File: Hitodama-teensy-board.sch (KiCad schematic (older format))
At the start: 16 parts, among them J1 Jack-DC, J2 Conn_01x20_Female, J3 Conn_01x20_Female, J4 Conn_01x20_Female, U4 Teensy3.6

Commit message: 2 row connector, routed on intermediate board
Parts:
- J2, J3, J4: footprint Connector_PinHeader_2.54mm:PinHeader_1x20_P2.54mm_Vertical -> Connector_IDC:IDC-Header_2x10_P2.54mm_Vertical
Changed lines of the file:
@@
 F 0 "J2" V 2265 4480 50  0000 C CNN
 F 1 "Conn_01x20_Female" V 2174 4480 50  0000 C CNN
-F 2 "Connector_PinHeader_2.54mm:PinHeader_1x20_P2.54mm_Vertical" H 2100 4550 50  0001 C CNN
+F 2 "Connector_IDC:IDC-Header_2x10_P2.54mm_Vertical" H 2100 4550 50  0001 C CNN
 F 3 "~" H 2100 4550 50  0001 C CNN
 	1    2100 4550
@@
 F 0 "J3" V 2265 5530 50  0000 C CNN
 F 1 "Conn_01x20_Female" V 2174 5530 50  0000 C CNN
-F 2 "Connector_PinHeader_2.54mm:PinHeader_1x20_P2.54mm_Vertical" H 2100 5600 50  0001 C CNN
+F 2 "Connector_IDC:IDC-Header_2x10_P2.54mm_Vertical" H 2100 5600 50  0001 C CNN
 F 3 "~" H 2100 5600 50  0001 C CNN
 	1    2100 5600
@@
 F 0 "J4" V 2215 6630 50  0000 C CNN
 F 1 "Conn_01x20_Female" V 2124 6630 50  0000 C CNN
-F 2 "Connector_PinHeader_2.54mm:PinHeader_1x20_P2.54mm_Vertical" H 2050 6700 50  0001 C CNN
+F 2 "Connector_IDC:IDC-Header_2x10_P2.54mm_Vertical" H 2050 6700 50  0001 C CNN
 F 3 "~" H 2050 6700 50  0001 C CNN
 	1    2050 6700

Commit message: trying different routing options teensy board
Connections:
- net VCC: now also U4.58 (5V)
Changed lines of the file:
@@
 	0    -1   -1   0
 $EndComp
+$Comp
+L power:VCC #PWR?
+U 1 1 5CE3B325
+P 8200 1600
+F 0 "#PWR?" H 8200 1450 50  0001 C CNN
+F 1 "VCC" V 8218 1727 50  0000 L CNN
+F 2 "" H 8200 1600 50  0001 C CNN
+F 3 "" H 8200 1600 50  0001 C CNN
+	1    8200 1600
+	1    0    0    -1
+$EndComp
 $EndSCHEMATC

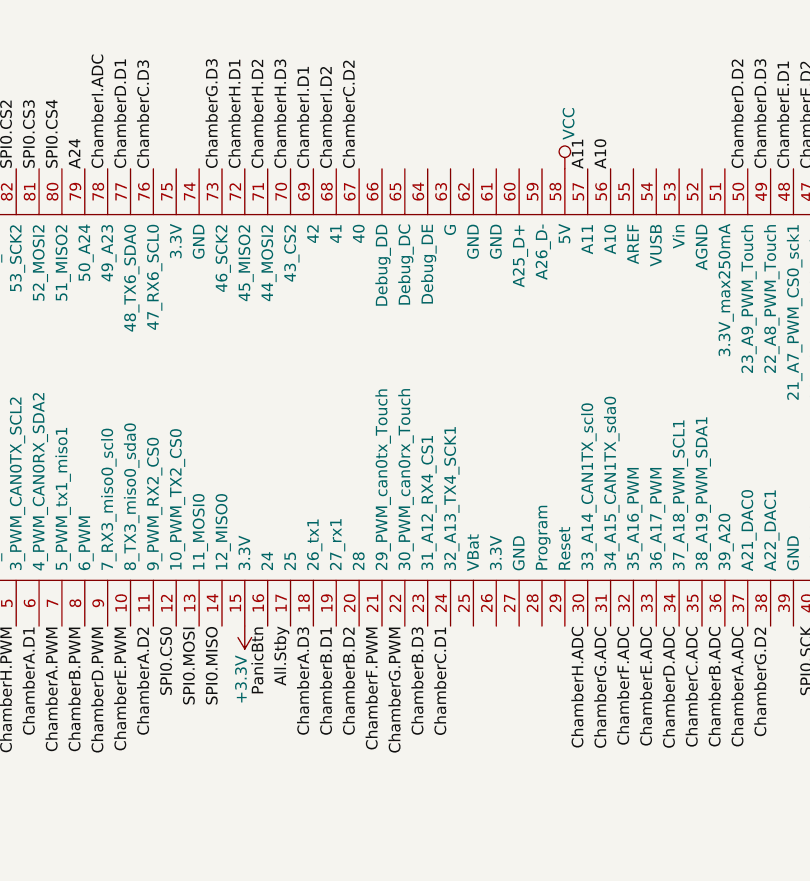
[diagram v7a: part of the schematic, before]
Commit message: fix cap wrong orientation & teensy vcc.
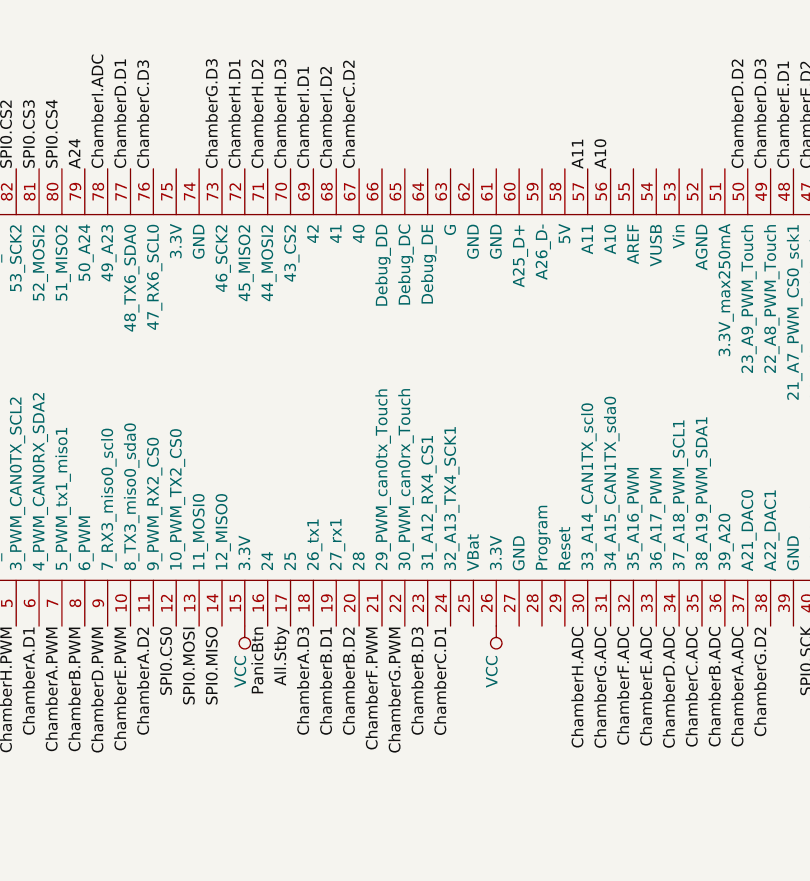
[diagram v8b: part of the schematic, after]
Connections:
- net +3V3 is gone; now on net VCC: U4.15 (3.3V)
- net VCC: now also U4.26 (3.3V); no longer U4.58 (5V)
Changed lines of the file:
@@
-	-1   0    0    1
-$EndComp
-$Comp
-L power:+3.3V #PWR0102
-U 1 1 5CBF166E
-P 6800 3600
-F 0 "#PWR0102" H 6800 3450 50  0001 C CNN
-F 1 "+3.3V" V 6815 3728 50  0000 L CNN
-F 2 "" H 6800 3600 50  0001 C CNN
-F 3 "" H 6800 3600 50  0001 C CNN
-	1    6800 3600
 	-1   0    0    1
 $EndComp
@@
 L power:VCC #PWR?
 U 1 1 5CE3B325
-P 8200 1600
-F 0 "#PWR?" H 8200 1450 50  0001 C CNN
-F 1 "VCC" V 8218 1727 50  0000 L CNN
-F 2 "" H 8200 1600 50  0001 C CNN
-F 3 "" H 8200 1600 50  0001 C CNN
-	1    8200 1600
-	1    0    0    -1
+P 7900 3600
+F 0 "#PWR?" H 7900 3450 50  0001 C CNN
+F 1 "VCC" V 7918 3727 50  0000 L CNN
+F 2 "" H 7900 3600 50  0001 C CNN
+F 3 "" H 7900 3600 50  0001 C CNN
+	1    7900 3600
+	-1   0    0    1
+$EndComp
+$Comp
+L power:VCC #PWR?
+U 1 1 5CF3FD56
+P 6800 3600
+F 0 "#PWR?" H 6800 3450 50  0001 C CNN
+F 1 "VCC" V 6818 3727 50  0000 L CNN
+F 2 "" H 6800 3600 50  0001 C CNN
+F 3 "" H 6800 3600 50  0001 C CNN
+	1    6800 3600
+	-1   0    0    1
 $EndComp
 $EndSCHEMATC
